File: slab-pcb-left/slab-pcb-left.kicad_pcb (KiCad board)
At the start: 2 copper layers, 171 x 103 mm, 183 parts, among them J1 Conn_01x04, J2 Conn_01x06, J3 Conn_01x06, J4 USB_C_Receptacle_USB2.0_16P, J5 AudioJack4, Q1 MMBT3906, SW1 RotaryEncoder, SW2 SW_Push, SW3 SW_Push, U1 RP2350_60QFN, U2 PCA9555PW, U3 PCA9555PW, U4 PCA9555PW, U5 SN74AHCT125PWR, U6 NCP1117-3.3_SOT223, U7 W25Q128JVS, Y1 ABM8-272-T3

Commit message: feat: route board
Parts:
- removed C35, C36, C37, C38, C39, C40, C49, C50, C51, C52, C58, C61: 100nF, Capacitor_SMD:C_0603_1608Metric_Pad1.08x0.95mm_HandSolder
- removed C53: 4.7uF, Capacitor_SMD:C_0402_1005Metric
- removed C54, C55: 4.7uF, CustomFootprints:C_0402_1005Metric_small_pads
- removed C56, C57: 15pF, Capacitor_SMD:C_0402_1005Metric
- removed C59, C60: 10uF, Capacitor_SMD:C_0805_2012Metric
- removed C62: 10u, Capacitor_SMD:C_0805_2012Metric
- removed L1: 3.3u, CustomFootprints:L_pol_2016
- removed LED32, LED33, LED34, LED35, LED36, LED37, LED38, LED39, LED40: MX_SK6812MINI-E, CustomFootprints:LED_MX_6028R-ROT_Custom
- removed LED49: SK6812MINI-E, CustomFootprints:LED_6028R_Custom
- removed MX31, MX32, MX33, MX34, MX35, MX36, MX37, MX38, MX39, MX40: MX_SW_HS, CustomFootprints:SW_choc_mx_combined
- removed R10: 33, Resistor_SMD:R_0402_1005Metric
- removed R11, R12: 27, Resistor_SMD:R_0402_1005Metric
- removed R13, R14: 2.2k, Resistor_SMD:R_0603_1608Metric_Pad0.98x0.95mm_HandSolder
- removed R15: 1k, Resistor_SMD:R_0603_1608Metric_Pad0.98x0.95mm_HandSolder
- removed R6: DNF, Resistor_SMD:R_0402_1005Metric
- removed R7: 10k, Resistor_SMD:R_0402_1005Metric
- removed R8, R9: 1k, Resistor_SMD:R_0402_1005Metric
- removed REF**: Xiao_rp2040_ACH, PCM_marbastlib-xp-promicroish:Xiao_rp2040_ACH
- removed SW2, SW3: SW_Push, Button_Switch_SMD:SW_Push_1P1T_XKB_TS-1187A
- removed TP10: NPIXEL_IN, TestPoint:TestPoint_Pad_1.0x1.0mm
- removed TP11: CC2, TestPoint:TestPoint_Pad_1.0x1.0mm
- removed TP208: QSPI_SS, TestPoint:TestPoint_Pad_1.0x1.0mm
- removed TP3: ENC_A, TestPoint:TestPoint_Pad_1.0x1.0mm
- removed TP4: ENC_B, TestPoint:TestPoint_Pad_1.0x1.0mm
- removed TP5: XIN, TestPoint:TestPoint_Pad_1.0x1.0mm
- removed TP6: XOUT, TestPoint:TestPoint_Pad_1.0x1.0mm
- removed TP7: RUN, TestPoint:TestPoint_Pad_1.0x1.0mm
- removed TP8: NPIXEL_SHIFT, TestPoint:TestPoint_Pad_1.0x1.0mm
- removed TP9: CC1, TestPoint:TestPoint_Pad_1.0x1.0mm
- removed U6: NCP1117-3.3_SOT223, Package_TO_SOT_SMD:SOT-223-3_TabPin2
- removed U7: W25Q128JVS, Package_SO:SOIC-8_5.23x5.23mm_P1.27mm
- removed Y1: ABM8-272-T3, Crystal:Crystal_SMD_3225-4Pin_3.2x2.5mm
- added H1: MountingHole_Pad, MountingHole:MountingHole_3.2mm_M3_Pad_TopBottom, F.Cu at (95.0, 87.5)
- added H2: MountingHole_Pad, MountingHole:MountingHole_3.2mm_M3_Pad_TopBottom, F.Cu at (133.0, 67.0)
- added H3: MountingHole_Pad, MountingHole:MountingHole_3.2mm_M3_Pad_TopBottom, F.Cu at (171.0, 114.0)
- added H4: MountingHole_Pad, MountingHole:MountingHole_3.2mm_M3_Pad_TopBottom, F.Cu at (114.0, 124.0)
- added H5: MountingHole_Pad, MountingHole:MountingHole_3.2mm_M3_Pad_TopBottom, F.Cu at (192.9, 123.5)
- added H6: MountingHole_Pad, MountingHole:MountingHole_3.2mm_M3_Pad_TopBottom, F.Cu at (76.0, 104.5)
- added H7: MountingHole_Pad, MountingHole:MountingHole_3.2mm_M3_Pad_TopBottom, F.Cu at (171.0, 76.0)
- added H8: MountingHole_Pad, MountingHole:MountingHole_3.2mm_M3_Pad_TopBottom, F.Cu at (60.8, 133.0)
- added H9: MountingHole_Pad, MountingHole:MountingHole_3.2mm_M3_Pad_TopBottom, F.Cu at (76.0, 71.5)
- added J6: Conn_01x06, Connector_PinHeader_2.54mm:PinHeader_1x06_P2.54mm_Vertical, F.Cu at (213.0, 149.3)
- J1: value Conn_01x04 -> MagnetR; footprint Connector_PinSocket_2.54mm:PinSocket_1x04_P2.54mm_Vertical -> CustomFootprints:5358_mag_connector_1x4_pads; moved to B.Cu
- J2: value Conn_01x06 -> MagnetL; footprint Connector_PinHeader_2.54mm:PinHeader_1x06_P2.54mm_Vertical -> CustomFootprints:5358_mag_connector_1x4_pins; moved to B.Cu
- J3: value Conn_01x06 -> TRRS_R; footprint Connector_PinHeader_2.54mm:PinHeader_1x06_P2.54mm_Vertical -> Connector_Audio:Jack_3.5mm_KoreanHropartsElec_PJ-320D-4A_Horizontal; moved to B.Cu
- J4: value USB_C_Receptacle_USB2.0_16P -> TRRS_L; footprint Connector_USB:USB_C_Receptacle_GCT_USB4105-xx-A_16P_TopMnt_Horizontal -> Connector_Audio:Jack_3.5mm_KoreanHropartsElec_PJ-320D-4A_Horizontal; moved to B.Cu
- J5: value AudioJack4 -> SSD1306; footprint Connector_Audio:Jack_3.5mm_KoreanHropartsElec_PJ-320D-4A_Horizontal -> CustomFootprints:SSD1306_128x32
- LED31: footprint CustomFootprints:LED_MX_6028R-ROT_Custom -> CustomFootprints:LED_6028R_Custom
- R1, R2: value 5.1k -> 2.2k
- R5: value 10k -> 1k
- TP1: value USB_DP -> NPIXEL_SHIFT
- TP2: value USB_DM -> NPIXEL_IN
- U1: value RP2350_60QFN -> Seeeduino Xiao rp2040; footprint RP2350:RP2350-QFN-60-1EP_7x7_P0.4mm_EP3.4x3.4mm_ThermalVias -> CustomFootprints:Xiao_rp2040_AC_Reflow_Custom; moved to B.Cu
- U4: value PCA9555PW -> ADS1110; footprint Package_SO:TSSOP-24_4.4x7.8mm_P0.65mm -> Package_TO_SOT_SMD:SOT-23-6_Handsoldering
- U5: value SN74AHCT125PWR -> PW14
- moved J5 271.4 mm to (202.5, 142.5), turned to 90 degrees
- moved LED7 208.1 mm to (171.0, 76.0)
- moved LED8 208.1 mm to (152.0, 76.0)
- moved MX7 208.1 mm to (171.0, 76.0)
- moved MX8 208.1 mm to (152.0, 76.0)
- moved RV1 181.9 mm to (64.7, 124.2)
- moved LED13 170.8 mm to (171.0, 95.0)
- moved LED14 170.8 mm to (152.0, 95.0)
- moved MX13 170.8 mm to (171.0, 95.0)
- moved MX14 170.8 mm to (152.0, 95.0)
- moved LED15 169.6 mm to (133.0, 88.5)
- moved MX15 169.6 mm to (133.0, 88.5)
- moved LED16 169.2 mm to (114.0, 86.0)
- moved MX16 169.2 mm to (114.0, 86.0)
- moved J3 167.2 mm to (63.4, 62.0)
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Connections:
- C32 pad 1: GND -> +3V3
- C32 pad 2: VBUS -> GND
- C33 pad 1: GND -> +3V3
- C33 pad 2: VBUS -> GND
- J1 pad 2: +3V3 -> /I2C0_SCL
- J1 pad 3: /I2C1_SCL -> /I2C0_SDA
- J1 pad 4: /I2C1_SDA -> VBUS
- J2 pad 1: VBUS -> GND
- J2 pad 2: /UART0_RX -> /I2C1_SCL
- J2 pad 3: /UART0_TX -> /I2C1_SDA
- J2 pad 4: GND -> VBUS
- LED31 pad 2: Net-(LED31-DOUT) -> unconnected-(LED31-DOUT-Pad2)
- R1 pad 1: Net-(J4-CC1) -> +3V3
- R1 pad 2: GND -> /I2C1_SDA
- R2 pad 1: Net-(J4-CC2) -> +3V3
- R2 pad 2: GND -> /I2C1_SCL
- R5 pad 1: +3V3 -> /BUZZER
- R5 pad 2: /EXPANDER3_INT -> Net-(Q1-B)
- RV1 pad 2: Net-(U1-GPIO26_ADC0) -> Net-(U4-VIN+)
- TP1 pad 1: /USB_D+ -> /KEY_PIXEL_SHIFT_INPUT
- TP2 pad 1: /USB_D- -> /KEY_PIXEL_INPUT
- U1 pad 1: unconnected-(U1-IOVDD-Pad1) -> /ENCODER_A
- U1 pad 10: /EXPANDER1_INT -> +3V3
- U1 pad 11: unconnected-(U1-IOVDD-Pad11) -> /EXPANDER2_INT
- U1 pad 12: /EXPANDER2_INT -> /KEY_PIXEL_SHIFT_INPUT
- U1 pad 13: /EXPANDER3_INT -> /BUZZER
- U1 pad 14: unconnected-(U1-GPIO10-Pad14) -> /UART0_RX
- U1 pad 2: /UART0_TX -> /ENCODER_B
- U1 pad 3: /UART0_RX -> /I2C0_SDA
- U1 pad 4: /ENCODER_A -> /I2C0_SCL
- U1 pad 5: /ENCODER_B -> /I2C1_SDA
- U1 pad 6: unconnected-(U1-DVDD-Pad6) -> /I2C1_SCL
- U1 pad 7: unconnected-(U1-GPIO4-Pad7) -> /UART0_TX
- U1 pad 8: unconnected-(U1-GPIO5-Pad8) -> VBUS
- U1 pad 9: /KEY_PIXEL_SHIFT_INPUT -> GND
- U2 pad 10: /KEY7 -> /KEY2
- U2 pad 11: /KEY8 -> /KEY3
- U2 pad 13: /KEY9 -> /KEY4
- U2 pad 14: /KEY10 -> /KEY5
- U2 pad 15: /KEY11 -> /KEY6
- U2 pad 16: /KEY12 -> /KEY10
- U2 pad 17: /KEY13 -> /KEY11
- U2 pad 18: /KEY14 -> /KEY12
- U2 pad 19: /KEY15 -> /KEY17
- U2 pad 4: /KEY1 -> /KEY15
- U2 pad 5: /KEY2 -> /KEY14
- U2 pad 6: /KEY3 -> /KEY7
- U2 pad 7: /KEY4 -> /KEY8
- U2 pad 8: /KEY5 -> /KEY9
- U2 pad 9: /KEY6 -> /KEY1
- U3 pad 10: /KEY23 -> /KEY19
- U3 pad 11: /KEY24 -> /KEY13
- U3 pad 13: /KEY25 -> /EXPANDER1_INT
- U3 pad 14: /KEY26 -> /KEY18
- U3 pad 15: /KEY27 -> /KEY24
- U3 pad 16: /KEY28 -> /KEY23
- U3 pad 17: /KEY29 -> /KEY22
- U3 pad 19: /KEY31 -> /KEY29
- U3 pad 20: /KEY32 -> /KEY28
- U3 pad 4: /KEY17 -> unconnected-(U3-IO0_0-Pad4)
- U3 pad 5: /KEY18 -> /KEY27
- U3 pad 6: /KEY19 -> /KEY26
- U3 pad 7: /KEY20 -> /KEY25
- U3 pad 9: /KEY22 -> /KEY20
- U4 pad 1: /EXPANDER3_INT -> Net-(U4-VIN+)
- U4 pad 2: +3V3 -> GND
- U4 pad 3: GND -> /I2C1_SCL
- U4 pad 4: /KEY33 -> /I2C1_SDA
- U4 pad 5: /KEY34 -> +3V3
- U4 pad 6: /KEY35 -> GND
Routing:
- net VBUS: track 2.00 -> 999.4 mm, vias 0 -> 35
- net /I2C1_SDA: track 0.00 -> 372.4 mm, vias 0 -> 14
- net /I2C1_SCL: track 0.00 -> 365.7 mm, vias 0 -> 10
- net GND: track 0.00 -> 279.6 mm, vias 0 -> 61
- net /I2C0_SDA: track 0.00 -> 238.9 mm, vias 0 -> 4
- net /ENCODER_A: track 0.00 -> 237.9 mm, vias 0 -> 5
- net /ENCODER_B: track 0.00 -> 232.4 mm, vias 0 -> 5
- net /I2C0_SCL: track 0.00 -> 230.0 mm, vias 0 -> 5
- net Net-(LED18-DOUT): track 0.00 -> 156.7 mm
- net +3V3: track 0.00 -> 151.2 mm, vias 0 -> 31
- net Net-(LED12-DOUT): track 0.00 -> 146.4 mm
- net Net-(LED6-DOUT): track 0.00 -> 145.5 mm
- net Net-(LED24-DOUT): track 0.00 -> 144.1 mm
- net /EXPANDER2_INT: track 0.00 -> 134.0 mm, vias 0 -> 4
- net /KEY13: track 0.00 -> 90.7 mm, vias 0 -> 2
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- added copper zone on B.Cu, net +3V3
- added copper zone on F.Cu, net GND
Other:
- board size 171 x 103 mm -> 158 x 104 mm
- board text added: "+5V"
- board text added: "GND"
- board text added: "RX"
- board text added: "SCL"
- board text added: "SDA"
- board text added: "TX"
- board text added: "VCC"

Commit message: feat: start right board
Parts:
- removed R5: 1k, Resistor_SMD:R_0603_1608Metric_Pad0.98x0.95mm_HandSolder
- U5: value PW14 -> SN74AHCT125PWR
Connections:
- BZ1 pad 1: VBUS -> Net-(BZ1-+)
- BZ1 pad 2: Net-(BZ1--) -> GND
- Q1 pad 1: Net-(Q1-B) -> /BUZZER
- Q1 pad 2: Net-(BZ1--) -> VBUS
- Q1 pad 3: GND -> Net-(BZ1-+)
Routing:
- net Net-(BZ1--): track 15.1 -> 0.00 mm
- net Net-(BZ1-+): track 0.00 -> 9.18 mm
- net /BUZZER: track 28.8 -> 33.8 mm
- net Net-(Q1-B): track 3.88 -> 0.00 mm
- net VBUS: track 999.4 -> 996.1 mm

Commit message: feat: full left and right boards
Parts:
- added REF**: WEEE-Logo_4.2x6mm_SilkScreen, Symbol:WEEE-Logo_4.2x6mm_SilkScreen, B.Cu at (205.3, 101.5)
- added REF**: OSHW-Logo2_7.3x6mm_SilkScreen, Symbol:OSHW-Logo2_7.3x6mm_SilkScreen, B.Cu at (199.2, 101.5)
- U5: value SN74AHCT125PWR -> PW14
- moved H6 5.00 mm to (76.0, 109.5)
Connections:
- BZ1 pad 3: (no net) -> GND
- BZ1 pad 4: (no net) -> GND
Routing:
- net VBUS: track 996.1 -> 999.0 mm
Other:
- board text added: "Debug Pins"
- board text added: "L"
- board text added: "NOW"
- board text added: "designed by edward h"
- board text added: "the slab keyboard"
- board text added: "version 3.0 'nowhere'"

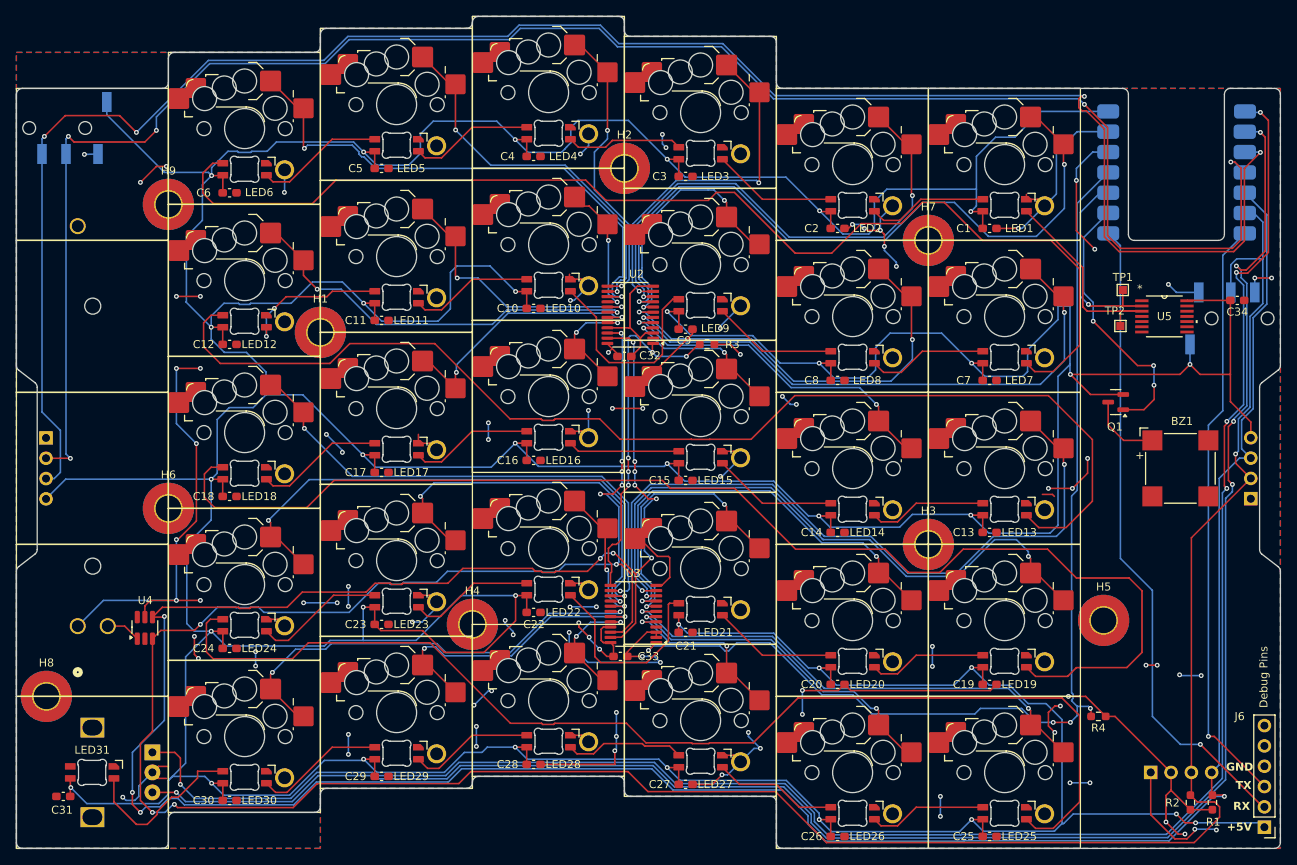
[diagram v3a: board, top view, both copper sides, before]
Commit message: feat: add hackpad
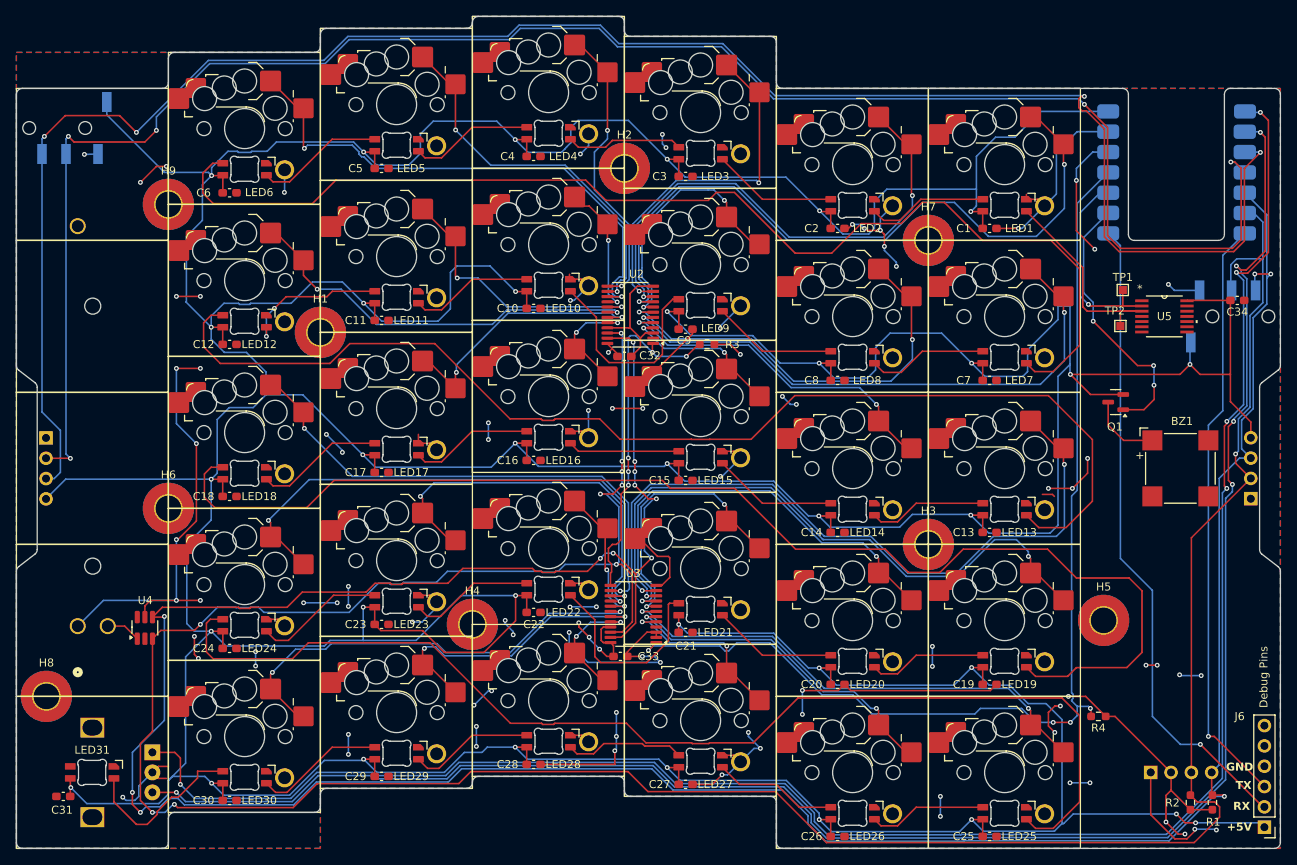
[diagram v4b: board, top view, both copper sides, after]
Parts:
- moved J4 0.27 mm to (208.8, 85.5)
